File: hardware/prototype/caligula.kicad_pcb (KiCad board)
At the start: 2 copper layers, 90 x 108.5 mm, 105 parts, among them J1 USB2UART, J10 PT100_CONN, J2 1.47 IPS LCD, J3 ConnBattery, J4 USB2UART, J5 lcd jumper, J6 lcd jumper, J7 lcd jumper, J8 PH Sensor, Q1 SS8050, Q2 SS8050, Q3 SS8050, SW1 RST, SW2 IN1, SW3 Boot, SW4 IN2, SW5 IN4, SW6 IN4, SW7 MST22D18G2, U1 CH340C, U2 ESP32-S3-WROOM-1, U3 TPS63001_SEPIC_3V3, U4 ICL7660, U5 BQ24075RGT_DPPM, U6 ADS1115IDGS, U7 MAX31865xTP, U8 OPA2197xD

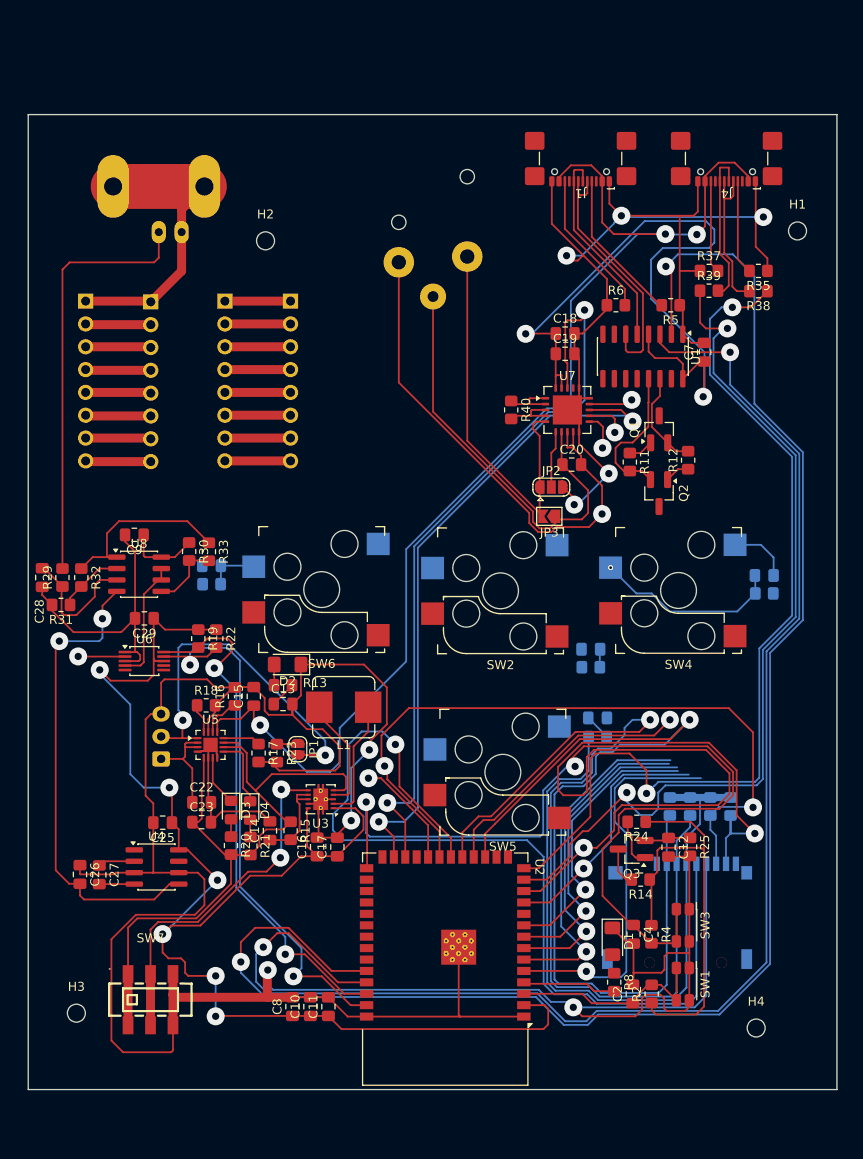
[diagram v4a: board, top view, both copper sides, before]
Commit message: feat: finish routing caligula proto v1
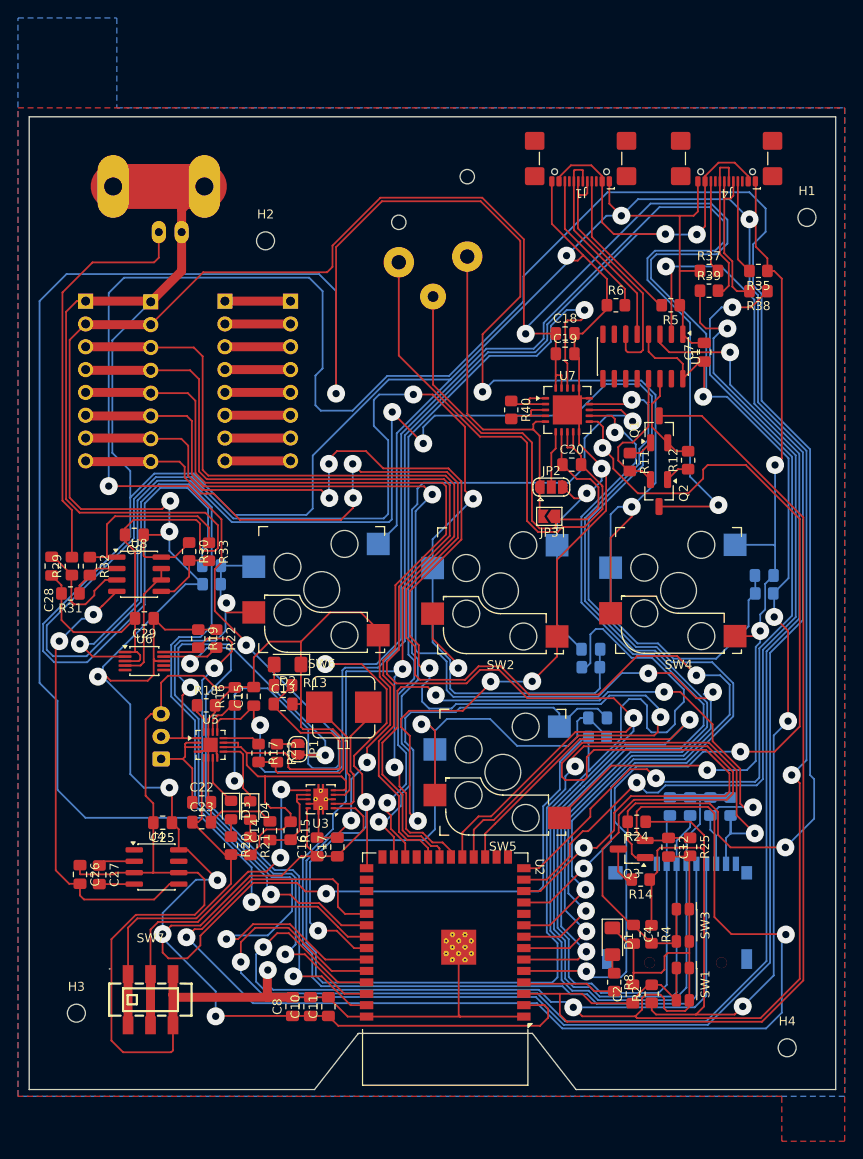
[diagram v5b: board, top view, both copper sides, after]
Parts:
- moved H4 4.09 mm to (124.6, 146.6)
- moved H1 1.83 mm to (126.8, 54.2)
- moved R31 1.65 mm to (44.8, 96.0)
- moved C28 1.65 mm to (42.8, 93.0)
- moved R29 1.65 mm to (45.0, 93.0)
- moved R32 1.59 mm to (47.0, 93.0)
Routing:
- net GND: track 551.1 -> 1104.7 mm, vias 9 -> 16
- net +3.3V: track 375.7 -> 691.2 mm, vias 8 -> 13
- net /~{CHG}: track 13.3 -> 310.5 mm, vias 0 -> 4
- net /IN2: track 21.0 -> 290.0 mm, vias 1 -> 4
- net /IN1: track 2.02 -> 236.5 mm, vias 0 -> 4
- net /IO0: track 101.4 -> 297.4 mm, vias 2 -> 4
- net /ADS1115_DRDY: track 33.0 -> 187.7 mm, vias 2 -> 4
- net Net-(Q3-E): track 5.12 -> 144.0 mm, vias 0 -> 2
- net /BLK: track 38.2 -> 158.2 mm, vias 1 -> 4
- net /DC: track 40.9 -> 147.9 mm, vias 1 -> 4
- net /EN: track 22.8 -> 126.7 mm
- net /CS: track 37.2 -> 140.0 mm, vias 1 -> 4
- net /SCK: track 110.8 -> 205.0 mm, vias 1 -> 2
- net /MOSI: track 108.4 -> 200.9 mm
- net /IN4: track 5.78 -> 84.3 mm, vias 0 -> 2
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- added copper zone on B.Cu, net (none)
- added copper zone on F.Cu, net (none)
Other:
- board size 90 x 108.5 mm -> 89.8 x 108.2 mm

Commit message: feat: rechecking routing
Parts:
- removed J10: PT100_CONN, Connector_Audio:Jack_XLR_Neutrik_NC3FAH1_Horizontal
- added H5: MountingHole, MountingHole:MountingHole_3.2mm_M3, F.Cu at (118.5, 146.8)
- added H6: MountingHole, MountingHole:MountingHole_3.2mm_M3, F.Cu at (125.2, 56.0)
- added H7: MountingHole, MountingHole:MountingHole_3.2mm_M3, F.Cu at (45.5, 138.2)
- added H8: MountingHole, MountingHole:MountingHole_3.2mm_M3, F.Cu at (44.2, 57.2)
- added J9: PT100_CONN, Connector_Audio:Jack_XLR_Neutrik_NC3FAH-0_Horizontal, B.Cu at (89.0, 58.6)
- moved H2 24.9 mm to (43.8, 46.8)
- moved H1 7.95 mm to (127.0, 46.2)
- moved H3 5.62 mm to (43.5, 148.0)
- moved H4 2.36 mm to (126.5, 148.0)
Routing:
- net GND: track 1104.7 -> 1084.6 mm, vias 16 -> 17
- net VDD: track 105.3 -> 89.3 mm
- net +3.3V: track 691.2 -> 697.1 mm
- net /TS: track 40.8 -> 44.6 mm
- net /IN1: track 236.5 -> 238.5 mm
- net /IN4: track 84.3 -> 82.5 mm
- net /BLK: track 158.2 -> 156.6 mm
- net /DC: track 147.9 -> 146.3 mm
- net /IO0: track 297.4 -> 298.7 mm
- net /I2C_SCL: track 61.4 -> 60.3 mm
- net /IN3: track 75.5 -> 76.4 mm
- net /MMC_CS: track 99.4 -> 100.1 mm
- net /I2C_SDA: track 65.1 -> 64.5 mm
- net /MISO: track 83.3 -> 83.9 mm
- net /CS: track 140.0 -> 139.5 mm
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
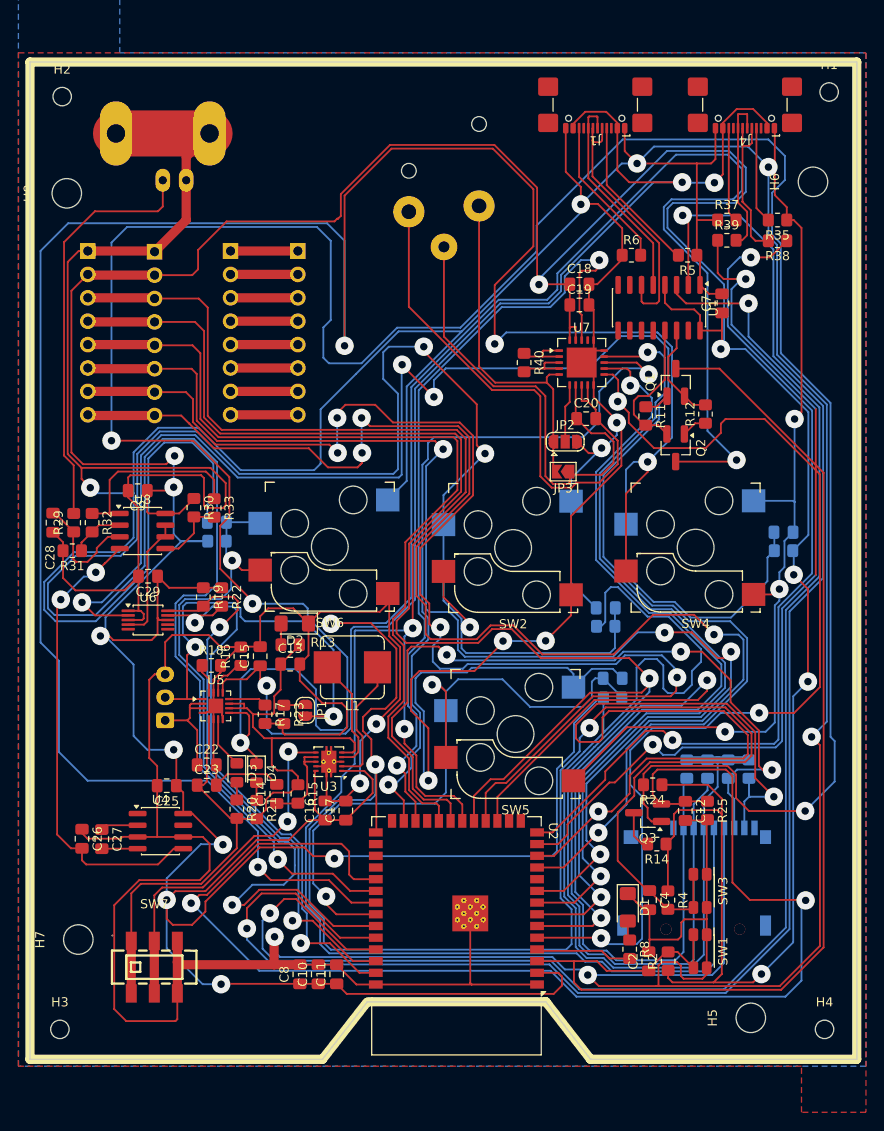
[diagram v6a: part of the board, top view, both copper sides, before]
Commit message: feat: reduce board size
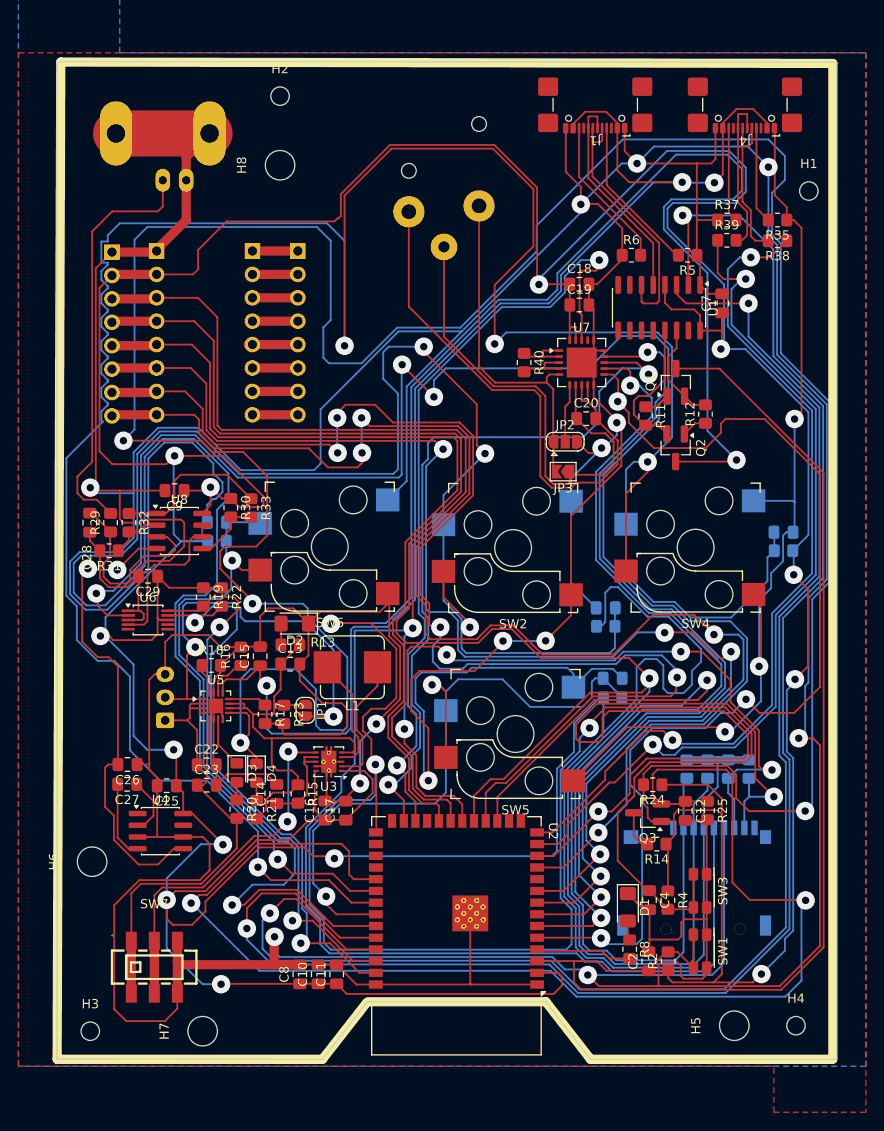
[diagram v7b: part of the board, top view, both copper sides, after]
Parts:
- moved H6 107.6 mm to (47.0, 129.8)
- moved H2 23.7 mm to (67.4, 46.7)
- moved H8 23.4 mm to (67.4, 54.2)
- moved H7 16.8 mm to (59.0, 148.2)
- moved H1 11.0 mm to (124.8, 57.0)
- moved C26 9.45 mm to (50.8, 119.2), turned to 180 degrees
- moved C27 6.55 mm to (50.8, 121.4), turned to 180 degrees
- moved C28 4.00 mm to (46.8, 93.0)
- moved C9 4.00 mm to (56.0, 89.5)
- moved R29 4.00 mm to (49.0, 93.0)
- moved R30 4.00 mm to (62.0, 91.4)
- moved R31 4.00 mm to (48.8, 96.0)
- moved R32 4.00 mm to (51.0, 93.0)
- moved R33 4.00 mm to (64.2, 91.4)
- moved U8 4.00 mm to (56.5, 93.9)
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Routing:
- net GND: track 1084.6 -> 1054.5 mm
- net Net-(U8A-+): track 12.7 -> 22.2 mm
- net +3.3V: track 697.1 -> 705.3 mm
- net /IN1: track 238.5 -> 233.4 mm
- net Net-(U4-CAP-): track 3.89 -> 8.46 mm
- net /~{CHG}: track 310.0 -> 314.4 mm
- net Net-(R32-Pad1): track 21.9 -> 17.6 mm
- net /IN2: track 289.8 -> 285.9 mm
- net VPH: track 13.7 -> 17.6 mm
- net /USB_DM: track 96.0 -> 93.4 mm
- net /USB_DP: track 96.2 -> 93.6 mm
- net /RESET: track 97.1 -> 94.6 mm
- net /CS: track 139.5 -> 137.0 mm
- net /DC: track 146.3 -> 143.7 mm
- net /MOSI: track 200.4 -> 197.8 mm
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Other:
- board size 89.8 x 108.2 mm -> 84.6 x 108.3 mm
